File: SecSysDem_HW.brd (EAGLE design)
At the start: 160 x 100 mm, 44 parts, among them J1 22-05-7078-07, J2 22-27-2021-02, T1 MOSFET_NCHANNEL_ENHANCEMENT2N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, T2 MOSFET_NCHANNEL_ENHANCEMENT2N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, T3 MOSFET_NCHANNEL_ENHANCEMENT2N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, U1 XPLAINED_MINI_PINOUT, U2 PCF8574_IO_EXPANDER, U3 MCP4706_DAC, U4 FT24C512A, X1 C-GRID-06-70553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

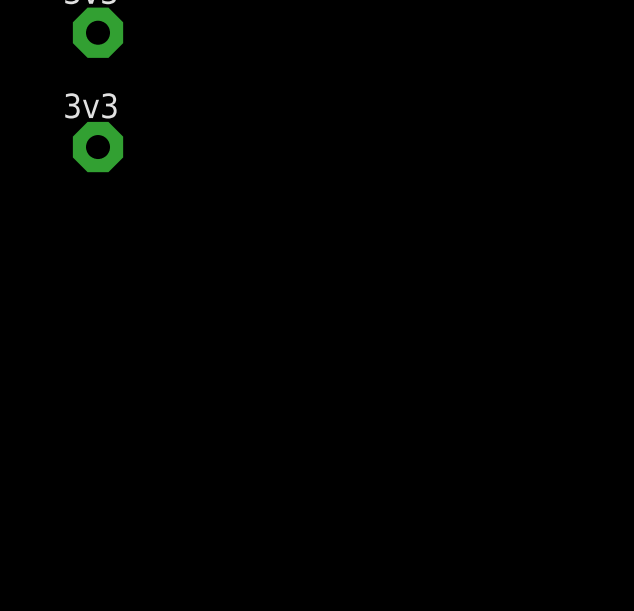
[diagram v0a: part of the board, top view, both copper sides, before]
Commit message: Added NPN transistor to power the LCD backlight
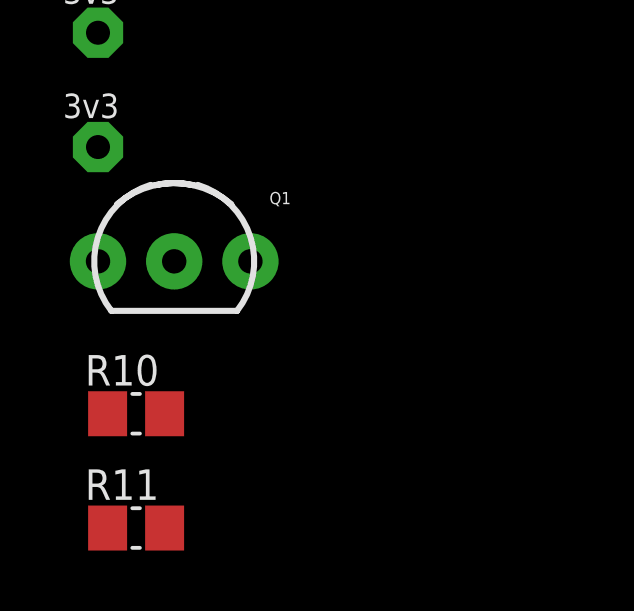
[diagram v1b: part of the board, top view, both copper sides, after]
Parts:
- added Q1: 2N3904, SparkFun-DiscreteSemi:TO-92-AMMO
- added R10: 1k, Luke:C0805
- added R11: 100, Luke:C0805
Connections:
- new net N$18: Q1.1, R11.2
- new net N$7: Q1.2, R10.2
- net +3V3: now also R11.1
- net LCD_BACKLIGHT: now also Q1.3, R10.1
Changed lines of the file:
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@@
 <element name="V8" library="Luke" package="VIA1" value="3v3" x="-184.15" y="-247.65"/>
 <element name="V9" library="Luke" package="VIA1" value="3v3" x="-184.15" y="-251.46"/>
+<element name="Q1" library="SparkFun-DiscreteSemi" package="TO-92-AMMO" value="2N3904" x="-181.61" y="-255.27"/>
+<element name="R10" library="Luke" package="C0805" value="1k" x="-182.88" y="-260.35"/>
+<element name="R11" library="Luke" package="C0805" value="100" x="-182.88" y="-264.16"/>
 </elements>
 <signals>
@@
 <contactref element="R7" pad="2"/>
 <contactref element="J2" pad="1"/>
+<contactref element="R11" pad="1"/>
 <wire x1="-173.04" y1="-118.11" x2="-166.37" y2="-85.09" width="0" layer="19" extent="1-1"/>
 <wire x1="-173.04" y1="-121.92" x2="-173.04" y2="-118.11" width="0" layer="19" extent="1-1"/>
@@
 <wire x1="-184.15" y1="-247.65" x2="-184.15" y2="-243.84" width="0" layer="19" extent="1-1"/>
 <wire x1="-184.15" y1="-251.46" x2="-184.15" y2="-247.65" width="0" layer="19" extent="1-1"/>
+<wire x1="-183.83" y1="-264.16" x2="-184.15" y2="-251.46" width="0" layer="19" extent="1-1"/>
 <wire x1="-130.81" y1="-68.58" x2="-166.37" y2="-85.09" width="0" layer="19" extent="1-1"/>
 <wire x1="-149.86" y1="-31.75" x2="-130.81" y2="-68.58" width="0" layer="19" extent="1-1"/>
@@
 <contactref element="U$3" pad="P$7" route="any" routetag="G$1.LIGHT"/>
 <contactref element="U$3" pad="P$15" route="any" routetag="G$1.LIGHT"/>
+<contactref element="Q1" pad="3"/>
+<contactref element="R10" pad="1"/>
+<wire x1="-179.07" y1="-255.27" x2="-183.83" y2="-260.35" width="0" layer="19" extent="1-1"/>
+<wire x1="-147.32" y1="-31.75" x2="-179.07" y2="-255.27" width="0" layer="19" extent="1-1"/>
 <wire x1="-36.83" y1="54.61" x2="-147.32" y2="7.25" width="0" layer="19" extent="1-1"/>
 </signal>
@@
 <wire x1="-181.61" y1="-167.91" x2="-180.34" y2="-181.61" width="0" layer="19" extent="1-1"/>
 </signal>
+<signal name="N$7">
+<contactref element="R10" pad="2"/>
+<contactref element="Q1" pad="2"/>
+<wire x1="-181.61" y1="-255.27" x2="-181.93" y2="-260.35" width="0" layer="19" extent="1-1"/>
+</signal>
+<signal name="N$18">
+<contactref element="Q1" pad="1"/>
+<contactref element="R11" pad="2"/>
+<wire x1="-184.15" y1="-255.27" x2="-181.93" y2="-264.16" width="0" layer="19" extent="1-1"/>
+</signal>
 </signals>

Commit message: Changed EEPROM address pins (A2, A1, A0) to VCC because of addressing conflicts with the RTC module on board EEPROM.
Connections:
- net +3V3: now also U2.1, U2.2, U2.3
- net GND: no longer U2.1, U2.2, U2.3
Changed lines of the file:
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@@
 <?xml version="1.0" encoding="utf-8"?>
 <!DOCTYPE eagle SYSTEM "eagle.dtd">
-<eagle version="6.5.0">
+<eagle version="7.3.0">
 <drawing>
 <settings>
@@
 <layer number="59" name="tCarbon" color="7" fill="1" visible="no" active="no"/>
 <layer number="60" name="bCarbon" color="7" fill="1" visible="no" active="no"/>
-<layer number="90" name="Modules" color="5" fill="1" visible="yes" active="yes"/>
+<layer number="90" name="Modules" color="5" fill="1" visible="no" active="no"/>
 <layer number="91" name="Nets" color="2" fill="1" visible="no" active="no"/>
 <layer number="92" name="Busses" color="1" fill="1" visible="no" active="no"/>
@@
 <pass name="Default">
 <param name="RoutingGrid" value="50mil"/>
+<param name="AutoGrid" value="1"/>
+<param name="Efforts" value="0"/>
+<param name="TopRouterVariant" value="1"/>
 <param name="tpViaShape" value="round"/>
 <param name="PrefDir.1" value="|"/>
@@
 <contactref element="S1" pad="2" route="any" routetag="G$1.1"/>
 <contactref element="C1" pad="2"/>
-<contactref element="U2" pad="1"/>
-<contactref element="U2" pad="2"/>
-<contactref element="U2" pad="3"/>
 <contactref element="U2" pad="8"/>
 <contactref element="JP1" pad="GNDBREAK"/>
@@
 <wire x1="-95.25" y1="-12.42" x2="-106.68" y2="-19.05" width="0" layer="19" extent="1-1"/>
 <wire x1="-90.45" y1="-9.62" x2="-95.25" y2="-12.42" width="0" layer="19" extent="1-1"/>
-<wire x1="-85.09" y1="-10.16" x2="-90.45" y2="-9.62" width="0" layer="19" extent="1-1"/>
-<wire x1="-82.55" y1="-10.16" x2="-85.09" y2="-10.16" width="0" layer="19" extent="1-1"/>
-<wire x1="-80.01" y1="-10.16" x2="-82.55" y2="-10.16" width="0" layer="19" extent="1-1"/>
-<wire x1="-67.31" y1="-10.16" x2="-80.01" y2="-10.16" width="0" layer="19" extent="1-1"/>
+<wire x1="-67.31" y1="-10.16" x2="-90.45" y2="-9.62" width="0" layer="19" extent="1-1"/>
 <wire x1="-44.45" y1="6.35" x2="-67.31" y2="-10.16" width="0" layer="19" extent="1-1"/>
 <wire x1="-23.18" y1="62.23" x2="-58.674" y2="54.61" width="0" layer="19" extent="1-1"/>
@@
 <contactref element="J2" pad="1"/>
 <contactref element="R11" pad="1"/>
+<contactref element="U2" pad="3"/>
+<contactref element="U2" pad="2"/>
+<contactref element="U2" pad="1"/>
 <wire x1="-173.04" y1="-118.11" x2="-166.37" y2="-85.09" width="0" layer="19" extent="1-1"/>
 <wire x1="-173.04" y1="-121.92" x2="-173.04" y2="-118.11" width="0" layer="19" extent="1-1"/>
@@
 <wire x1="-149.86" y1="-31.75" x2="-130.81" y2="-68.58" width="0" layer="19" extent="1-1"/>
 <wire x1="-85.09" y1="-2.54" x2="-149.86" y2="7.25" width="0" layer="19" extent="1-1"/>
-<wire x1="-49.53" y1="6.35" x2="-85.09" y2="-2.54" width="0" layer="19" extent="1-1"/>
+<wire x1="-85.09" y1="-10.16" x2="-85.09" y2="-2.54" width="0" layer="19" extent="1-1"/>
+<wire x1="-82.55" y1="-10.16" x2="-85.09" y2="-10.16" width="0" layer="19" extent="1-1"/>
+<wire x1="-80.01" y1="-10.16" x2="-82.55" y2="-10.16" width="0" layer="19" extent="1-1"/>
+<wire x1="-49.53" y1="6.35" x2="-80.01" y2="-10.16" width="0" layer="19" extent="1-1"/>
 </signal>
 <signal name="PHOTORESISTOR">

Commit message: Started the pcb layout. PCB made to fit the TaydaElectronics.com plastic box
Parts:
- moved S2 285.4 mm to (77.0, 11.0), turned to 270 degrees
- moved U$3 236.8 mm to (77.0, 22.0)
- moved X1 166.7 mm to (12.0, 31.0), flipped to the bottom, turned to 90 degrees
- moved IC1 145.0 mm to (23.7, 48.2), turned to 180 degrees
- moved JP1 144.7 mm to (17.8, 70.0), flipped to the bottom, turned to 180 degrees
- moved J1 137.1 mm to (21.9, 16.4), flipped to the bottom
- moved U2 127.5 mm to (40.8, 44.4), flipped to the bottom, turned to 180 degrees
- moved U1 53.9 mm to (32.3, 6.66), flipped to the bottom
- moved S1 25.4 mm to (7.00, 59.0), flipped to the bottom
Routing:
- added copper zone on layer 16, net +3V3
- added copper zone on layer 1, net GND
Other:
- board size 160 x 100 mm -> 99 x 65 mm

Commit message: Added flyback diode to solenoid. Changed most connectors to verticle. Continued PCB layout and increased PCB size.
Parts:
- removed J1: 22-05-7078-07, con-molex:7395-07
- removed J2: 22-27-2021-02, con-molex:6410-02
- removed X2, X3, X6: C-GRID-03-70553, con-molex:70553-03
- removed X4: C-GRID-04-70553, con-molex:70553-04
- added D1: 1N5819-T, diode:DO41-7.6
- added JP2, JP3, JP4: (no value), SparkFun-Connectors:1X03
- added JP5: (no value), SparkFun-Connectors:1X02
- added JP6: (no value), SparkFun-Connectors:1X04
- added JP7: (no value), SparkFun-Connectors:1X07
- moved R11 324.8 mm to (5.88, 0.16), turned to 180 degrees
- moved C4 295.5 mm to (83.0, 10.0), turned to 180 degrees
- moved R3 266.8 mm to (71.0, 7.79), turned to 180 degrees
- moved U4 265.2 mm to (9.66, -5.50)
- moved R2 264.2 mm to (71.0, 4.98), turned to 180 degrees
- moved R1 261.1 mm to (71.0, 0.00), turned to 180 degrees
- moved R6 257.9 mm to (14.2, 10.1), turned to 90 degrees
- moved X8 256.0 mm to (1.93, -26.0)
- moved U3 253.0 mm to (17.1, -6.29)
- moved T1 232.4 mm to (18.0, 30.0), turned to 90 degrees
- moved R4 227.0 mm to (21.1, -1.99), turned to 90 degrees
- moved R5 226.4 mm to (18.1, -2.01), turned to 270 degrees
- moved X5 224.1 mm to (7.24, 25.2), turned to 270 degrees
- moved T2 218.5 mm to (-25.6, -15.9)
- moved R10 209.3 mm to (-47.9, -100.3)
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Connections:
- removed net SPI_MISO: U1.P$27
- new net N$19: Q1.3, U$3.P$15, U$3.P$7
- net +3V3: now also JP5.1, JP6.3; no longer J2.1, X4.3
- net +5V: now also JP2.1, JP3.1, JP4.3; no longer X2.1, X3.1, X6.3
- net DOOR_HALL_EFFECT: now also JP2.3; no longer X3.3
- net GND: now also JP2.2, JP3.2, JP4.1; no longer X2.2, X3.2, X6.1
- net KEYPAD_1: now also JP7.1; no longer J1.1
- net KEYPAD_2: now also JP7.2; no longer J1.2
- net KEYPAD_3: now also JP7.3; no longer J1.3
- net KEYPAD_4: now also JP7.4; no longer J1.4
- net KEYPAD_5: now also JP7.5; no longer J1.5
- net KEYPAD_6: now also JP7.6; no longer J1.6
- net KEYPAD_7: now also JP7.7; no longer J1.7
- net LCD_BACKLIGHT: no longer Q1.3, U$3.P$15, U$3.P$7
- net N$1: now also D1.A
- net N$17: now also D1.C
- net N$2: now also JP6.4; no longer X4.4
- net N$4: now also JP6.2; no longer X4.2
- net N$5: now also JP6.1; no longer X4.1
- net PHOTORESISTOR: now also JP5.2; no longer J2.2
- net PIR_SENSOR: now also JP4.2; no longer X6.2
- net WINDOW_HALL_EFFECT: now also JP3.3; no longer X2.3
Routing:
- added copper zone on layer 16, net GND
- removed copper zone on layer 16, net +3V3
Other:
- board size 99 x 65 mm -> 99 x 80 mm

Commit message: Changed DAC to MCP4901-E/SN because the package was too small.
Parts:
- removed U3: MCP4706_DAC, Luke:SOT23-6
- removed V2: PB2, Luke:VIA1
- added U5: MCP4901-E/SN, Luke:8-SOIC
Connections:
- removed net N$12: U1.P$25, V2.P$1
- new net !DAC_CS: U1.P$25, U5.2
- net +3V3: now also U5.1; no longer U3.3
- net GND: now also U5.7; no longer U3.2
- net I2C_SCL: no longer U3.5
- net I2C_SDA: no longer U3.4
- net N$3: now also U5.8; no longer U3.1
- net SPI_MOSI: now also U5.4
- net SPI_SCK: now also U5.3
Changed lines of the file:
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@@
 <element name="C4" library="Luke" package="C0805" value="1uF" x="83" y="10" rot="R180"/>
 <element name="R6" library="Luke" package="C0805" value="2.2k" x="14.21" y="10.12" rot="R90"/>
-<element name="U3" library="Luke" package="SOT23-6" value="MCP4706_DAC" x="17.12" y="-6.29"/>
 <element name="T2" library="Luke" package="SOT23" value="MOSFET_NCHANNEL_ENHANCEMENT2N7002,215" x="-25.61" y="-15.91">
 <attribute name="ID" value="300 mA" x="-25.61" y="-15.91" size="1.778" layer="27" display="off"/>
@@
 </element>
 <element name="R9" library="Luke" package="C0805" value="0R" x="-47.88" y="-60.98"/>
-<element name="V2" library="Luke" package="VIA1" value="PB2" x="-49.15" y="-64.79"/>
 <element name="V3" library="Luke" package="VIA1" value="TXD" x="-49.15" y="-68.6"/>
 <element name="V4" library="Luke" package="VIA1" value="RXD" x="-49.15" y="-72.41"/>
@@
 <element name="JP6" library="SparkFun-Connectors" package="1X04" value="" x="67" y="8" rot="R270"/>
 <element name="JP7" library="SparkFun-Connectors" package="1X07" value="" x="53" y="6" rot="R180"/>
+<element name="U5" library="Luke" package="8-SOIC" value="MCP4901-E/SN" x="28" y="-6"/>
 </elements>
 <signals>
@@
 <contactref element="C4" pad="2"/>
 <contactref element="R6" pad="1"/>
-<contactref element="U3" pad="2"/>
 <contactref element="T2" pad="2"/>
 <contactref element="U4" pad="4"/>
@@
 <vertex x="-1" y="70"/>
 </polygon>
+<contactref element="U5" pad="7"/>
+<wire x1="-45.66" y1="-55.63" x2="27.365" y2="-3.4" width="0" layer="19" extent="1-1"/>
 <wire x1="-24.66" y1="-16.91" x2="-45.66" y2="-55.63" width="0" layer="19" extent="1-1"/>
 <wire x1="7.755" y1="-8.1" x2="-24.66" y2="-16.91" width="0" layer="19" extent="1-1"/>
-<wire x1="17.12" y1="-7.44" x2="11.565" y2="-8.1" width="0" layer="19" extent="1-1"/>
+<wire x1="9.025" y1="-8.1" x2="7.755" y2="-8.1" width="0" layer="19" extent="1-1"/>
+<wire x1="10.295" y1="-8.1" x2="9.025" y2="-8.1" width="0" layer="19" extent="1-1"/>
+<wire x1="11.565" y1="-8.1" x2="10.295" y2="-8.1" width="0" layer="19" extent="1-1"/>
+<wire x1="14.21" y1="9.17" x2="11.565" y2="-8.1" width="0" layer="19" extent="1-1"/>
+<wire x1="23.3" y1="23.53" x2="14.21" y2="9.17" width="0" layer="19" extent="1-1"/>
+<wire x1="19" y1="30.95" x2="23.3" y2="23.53" width="0" layer="19" extent="1-1"/>
+<wire x1="27.1" y1="32.11" x2="19" y2="30.95" width="0" layer="19" extent="1-1"/>
+<wire x1="14.27" y1="39.94" x2="19" y2="30.95" width="0" layer="19" extent="1-1"/>
+<wire x1="14.27" y1="47.13" x2="14.27" y2="39.94" width="0" layer="19" extent="1-1"/>
+<wire x1="21.05" y1="42.96" x2="14.27" y2="39.94" width="0" layer="19" extent="1-1"/>
+<wire x1="22.55" y1="59.3" x2="14.27" y2="47.13" width="0" layer="19" extent="1-1"/>
+<wire x1="17.75" y1="62.1" x2="22.55" y2="59.3" width="0" layer="19" extent="1-1"/>
+<wire x1="10.2512" y1="65.2606" x2="17.75" y2="62.1" width="0" layer="19" extent="1-1"/>
+<wire x1="7" y1="63.95" x2="10.2512" y2="65.2606" width="0" layer="19" extent="1-1"/>
+<wire x1="33.54" y1="64" x2="22.55" y2="59.3" width="0" layer="19" extent="1-1"/>
+<wire x1="42.54" y1="19" x2="23.3" y2="23.53" width="0" layer="19" extent="1-1"/>
+<wire x1="64.58" y1="15.66" x2="42.54" y2="19" width="0" layer="19" extent="1-1"/>
+<wire x1="85.89" y1="59" x2="81.344" y2="63.92" width="0" layer="19" extent="1-1"/>
+<wire x1="82.05" y1="10" x2="85.89" y2="20" width="0" layer="19" extent="1-1"/>
+<wire x1="80.7394" y1="7.2512" x2="82.05" y2="10" width="0" layer="19" extent="1-1"/>
+<wire x1="60" y1="2" x2="64.58" y2="15.66" width="0" layer="19" extent="1-1"/>
 </signal>
 <signal name="I2C_SDA">
@@
 <contactref element="X1" pad="3"/>
 <contactref element="R4" pad="1"/>
-<contactref element="U3" pad="4"/>
 <contactref element="U4" pad="5"/>
 <wire x1="30.92" y1="8.29" x2="46.8" y2="15.66" width="0" layer="19" extent="1-1"/>
 <wire x1="21.11" y1="-2.94" x2="30.92" y2="8.29" width="0" layer="19" extent="1-1"/>
-<wire x1="18.07" y1="-5.14" x2="21.11" y2="-2.94" width="0" layer="19" extent="1-1"/>
-<wire x1="11.565" y1="-2.9" x2="18.07" y2="-5.14" width="0" layer="19" extent="1-1"/>
+<wire x1="11.565" y1="-2.9" x2="21.11" y2="-2.94" width="0" layer="19" extent="1-1"/>
 <wire x1="27.1" y1="37.19" x2="30.92" y2="8.29" width="0" layer="19" extent="1-1"/>
 </signal>
@@
 <contactref element="X1" pad="4"/>
 <contactref element="R5" pad="1"/>
-<contactref element="U3" pad="5"/>
 <contactref element="U4" pad="6"/>
 <wire x1="30.92" y1="10.83" x2="27.1" y2="39.73" width="0" layer="19" extent="1-1"/>
 <wire x1="44.26" y1="15.66" x2="30.92" y2="10.83" width="0" layer="19" extent="1-1"/>
 <wire x1="18.08" y1="-1.06" x2="30.92" y2="10.83" width="0" layer="19" extent="1-1"/>
-<wire x1="17.12" y1="-5.14" x2="18.08" y2="-1.06" width="0" layer="19" extent="1-1"/>
-<wire x1="10.295" y1="-2.9" x2="17.12" y2="-5.14" width="0" layer="19" extent="1-1"/>
+<wire x1="10.295" y1="-2.9" x2="18.08" y2="-1.06" width="0" layer="19" extent="1-1"/>
 </signal>
 <signal name="!RESET_BTN">
@@
 <contactref element="U$3" pad="P$13" route="any" routetag="G$1.CLK"/>
 <contactref element="U$3" pad="P$5" route="any" routetag="G$1.CLK"/>
-<wire x1="78.27" y1="59" x2="78.804" y2="63.92" width="0" layer="19" extent="1-1"/>
+<contactref element="U5" pad="3"/>
+<wire x1="78.27" y1="20" x2="28.635" y2="-8.6" width="0" layer="19" extent="1-1"/>
+<wire x1="78.804" y1="63.92" x2="78.27" y2="59" width="0" layer="19" extent="1-1"/>
 </signal>
 <signal name="SPI_MOSI">
@@
 <contactref element="U$3" pad="P$4" route="any" routetag="G$1.DIN"/>
 <contactref element="U$3" pad="P$12" route="any" routetag="G$1.DIN"/>
-<wire x1="75.73" y1="59" x2="73.724" y2="63.92" width="0" layer="19" extent="1-1"/>
+<contactref element="U5" pad="4"/>
+<wire x1="75.73" y1="20" x2="29.905" y2="-8.6" width="0" layer="19" extent="1-1"/>
+<wire x1="73.724" y1="63.92" x2="75.73" y2="59" width="0" layer="19" extent="1-1"/>
 </signal>
 <signal name="+5V">
@@
 <contactref element="R5" pad="2"/>
 <contactref element="R4" pad="2"/>
-<contactref element="U3" pad="3"/>
 <contactref element="U4" pad="8"/>
 <contactref element="V7" pad="P$1"/>
@@
 <contactref element="JP5" pad="1"/>
 <contactref element="JP6" pad="3"/>
+<contactref element="U5" pad="1"/>
+<wire x1="-49.15" y1="-91.46" x2="26.095" y2="-8.6" width="0" layer="19" extent="1-1"/>
 <wire x1="-49.15" y1="-87.65" x2="-49.15" y2="-91.46" width="0" layer="19" extent="1-1"/>
 <wire x1="-49.15" y1="-83.84" x2="-49.15" y2="-87.65" width="0" layer="19" extent="1-1"/>
@@
 <wire x1="18.08" y1="-2.96" x2="7.755" y2="-2.9" width="0" layer="19" extent="1-1"/>
 <wire x1="21.11" y1="-1.04" x2="18.08" y2="-2.96" width="0" layer="19" extent="1-1"/>
-<wire x1="18.07" y1="-7.44" x2="18.08" y2="-2.96" width="0" layer="19" extent="1-1"/>
 <wire x1="23.3" y1="5.75" x2="21.11" y2="-1.04" width="0" layer="19" extent="1-1"/>
 <wire x1="23.3" y1="8.29" x2="23.3" y2="5.75" width="0" layer="19" extent="1-1"/>
@@
 </signal>
 <signal name="N$3">
-<contactref element="U3" pad="1"/>
 <contactref element="T2" pad="1"/>
-<wire x1="16.17" y1="-7.44" x2="-26.56" y2="-16.91" width="0" layer="19" extent="1-1"/>
+<contactref element="U5" pad="8"/>
+<wire x1="-26.56" y1="-16.91" x2="26.095" y2="-3.4" width="0" layer="19" extent="1-1"/>
 </signal>
 <signal name="N$8">
@@
 <contactref element="V1" pad="P$1"/>
 <wire x1="9.025" y1="-2.9" x2="-49.15" y2="-36.85" width="0" layer="19" extent="1-1"/>
-</signal>
-<signal name="N$12">
-<contactref element="U1" pad="P$25"/>
-<contactref element="V2" pad="P$1"/>
-<wire x1="-49.15" y1="-64.79" x2="71.184" y2="63.92" width="0" layer="19" extent="1-1"/>
 </signal>
 <signal name="N$13">
@@
 <wire x1="83.35" y1="20" x2="-44.07" y2="-95.27" width="0" layer="19" extent="1-1"/>
 </signal>
+<signal name="!DAC_CS">
+<contactref element="U5" pad="2"/>
+<contactref element="U1" pad="P$25"/>
+<wire x1="71.184" y1="63.92" x2="27.365" y2="-8.6" width="0" layer="19" extent="1-1"/>
+</signal>
 </signals>
